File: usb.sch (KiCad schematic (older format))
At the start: 17 parts, among them J4 CONN_02X03, U1 LFE5U-85F-6BG381C, Y1 FNETHE025

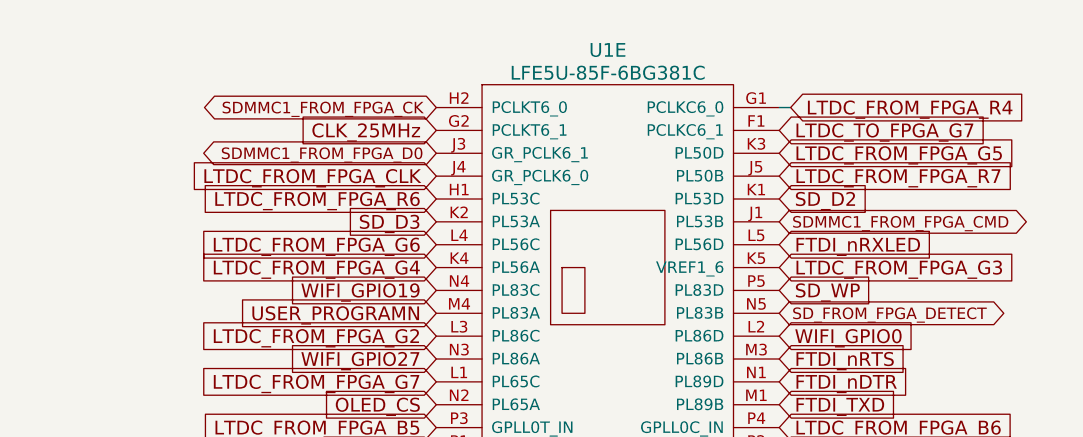
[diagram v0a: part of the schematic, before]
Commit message: Adding SPI from FPGA
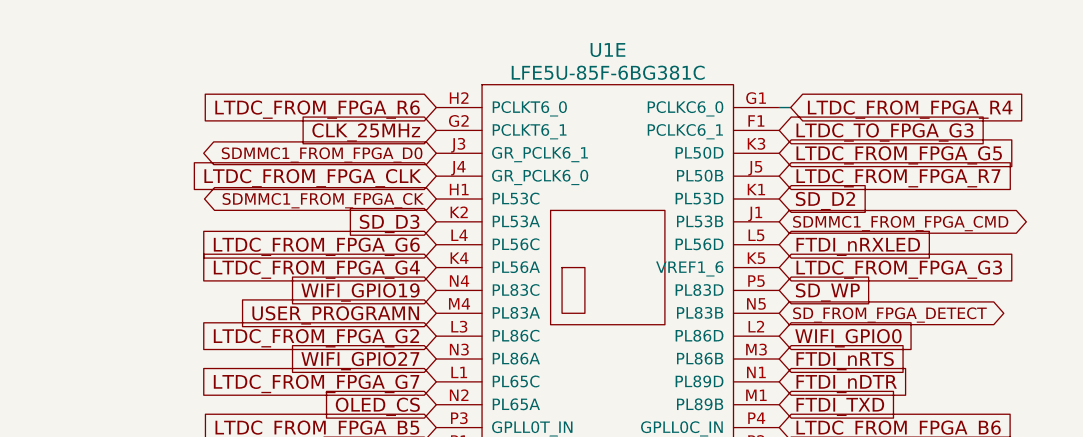
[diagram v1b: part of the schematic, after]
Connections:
- net LTDC_FROM_FPGA_R6: now also U1.H2 (PCLKT6_0); no longer U1.H1 (PL53C)
- net SDMMC1_FROM_FPGA_CK: now also U1.H1 (PL53C); no longer U1.H2 (PCLKT6_0)
- net LTDC_TO_FPGA_G7 renamed LTDC_TO_FPGA_G3
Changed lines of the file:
@@
 Text GLabel 10200 1350 2    60   Input ~ 0
 LTDC_FROM_FPGA_R4
-Text GLabel 8650 1750 0    60   Input ~ 0
+Text GLabel 8650 1350 0    60   Input ~ 0
 LTDC_FROM_FPGA_R6
 Text GLabel 8650 1650 0    60   Input ~ 0
@@
 Text GLabel 8650 1550 0    50   BiDi ~ 0
 SDMMC1_FROM_FPGA_D0
-Text GLabel 8650 1350 0    50   BiDi ~ 0
+Text GLabel 8650 1750 0    50   BiDi ~ 0
 SDMMC1_FROM_FPGA_CK
 Text GLabel 10150 1450 2    60   Input ~ 0
-LTDC_TO_FPGA_G7
+LTDC_TO_FPGA_G3
 $EndSCHEMATC

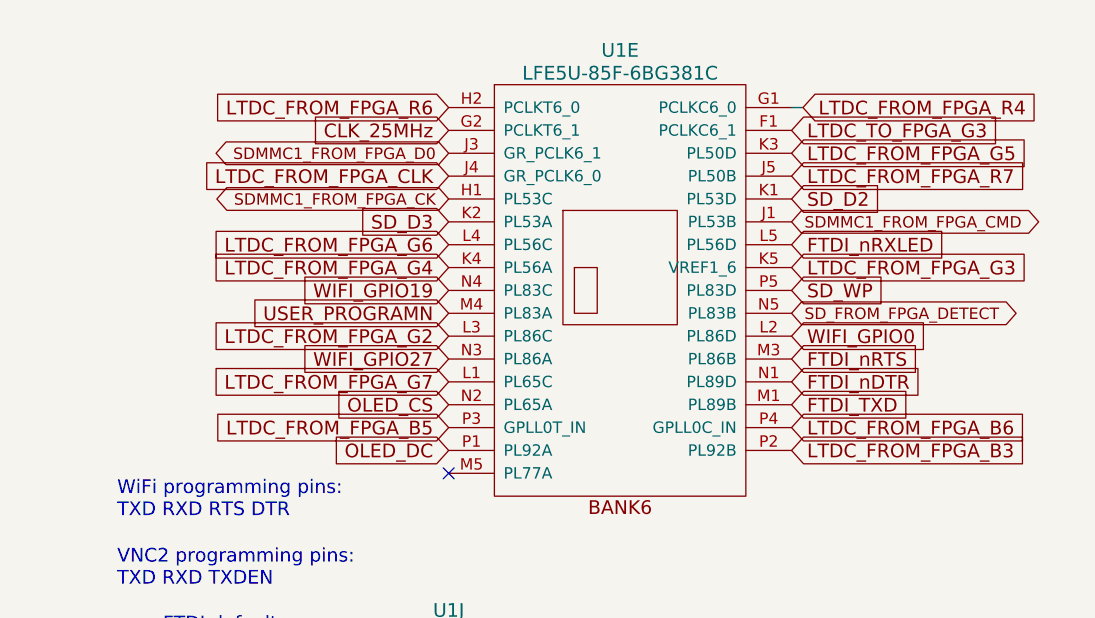
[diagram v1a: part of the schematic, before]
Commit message: Routing FPGA to LCD
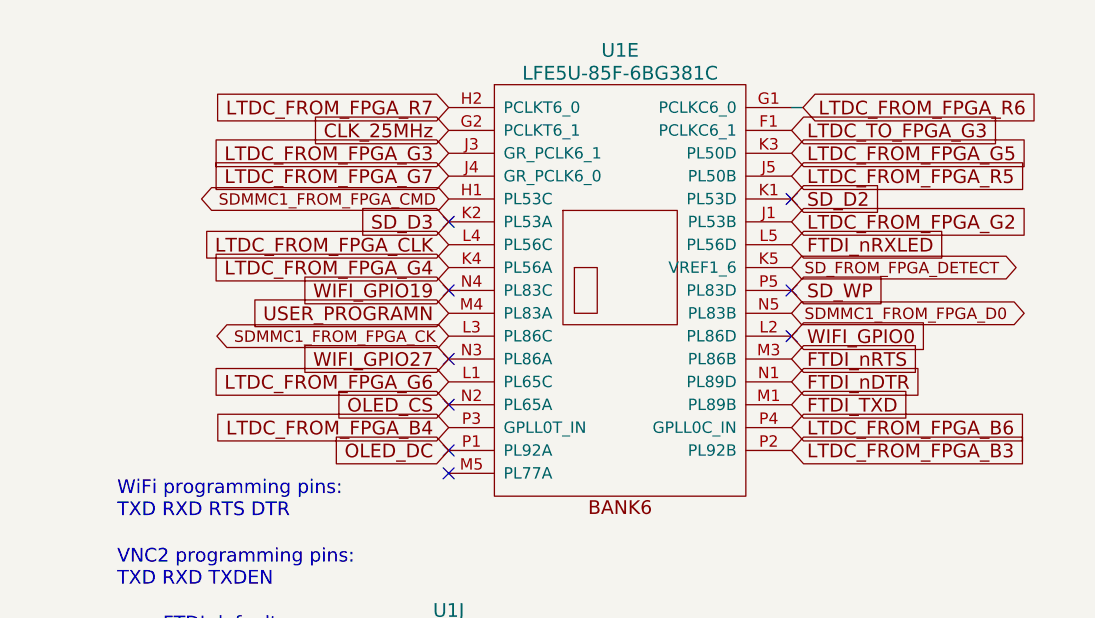
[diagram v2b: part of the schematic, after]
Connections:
- net LTDC_FROM_FPGA_R4 is gone; now on net LTDC_FROM_FPGA_R6: U1.G1 (PCLKC6_0)
- net LTDC_FROM_FPGA_CLK: now also U1.L4 (PL56C); no longer U1.J4 (GR_PCLK6_0)
- net LTDC_FROM_FPGA_G2: now also U1.J1 (PL53B); no longer U1.L3 (PL86C)
- net LTDC_FROM_FPGA_G3: now also U1.J3 (GR_PCLK6_1); no longer U1.K5 (VREF1_6)
- net LTDC_FROM_FPGA_G6: now also U1.L1 (PL65C); no longer U1.L4 (PL56C)
- net LTDC_FROM_FPGA_G7: now also U1.J4 (GR_PCLK6_0); no longer U1.L1 (PL65C)
- net LTDC_FROM_FPGA_R6: no longer U1.H2 (PCLKT6_0)
- net LTDC_FROM_FPGA_R7: now also U1.H2 (PCLKT6_0); no longer U1.J5 (PL50B)
- net SDMMC1_FROM_FPGA_CK: now also U1.L3 (PL86C); no longer U1.H1 (PL53C)
- net SDMMC1_FROM_FPGA_CMD: now also U1.H1 (PL53C); no longer U1.J1 (PL53B)
- net SDMMC1_FROM_FPGA_D0: now also U1.N5 (PL83B); no longer U1.J3 (GR_PCLK6_1)
- net SD_FROM_FPGA_DETECT: now also U1.K5 (VREF1_6); no longer U1.N5 (PL83B)
- net LTDC_FROM_FPGA_B5 renamed LTDC_FROM_FPGA_B4
- new net LTDC_FROM_FPGA_R5: U1.J5 (PL50B)
- no-connect marks 1 -> 9
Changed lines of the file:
@@
 LTDC_FROM_FPGA_B6
 Text GLabel 10200 1350 2    60   Input ~ 0
-LTDC_FROM_FPGA_R4
-Text GLabel 8650 1350 0    60   Input ~ 0
 LTDC_FROM_FPGA_R6
-Text GLabel 8650 1650 0    60   Input ~ 0
+Text GLabel 8650 1950 0    60   Input ~ 0
 LTDC_FROM_FPGA_CLK
-Text GLabel 8650 2550 0    60   Input ~ 0
-LTDC_FROM_FPGA_G7
-Text GLabel 8650 1950 0    60   Input ~ 0
-LTDC_FROM_FPGA_G6
 Text GLabel 10150 1550 2    60   Input ~ 0
 LTDC_FROM_FPGA_G5
-Text GLabel 10150 2050 2    60   Input ~ 0
-LTDC_FROM_FPGA_G3
-Text GLabel 8650 2350 0    60   Input ~ 0
+Text GLabel 10150 1850 2    60   Input ~ 0
 LTDC_FROM_FPGA_G2
-Text GLabel 8650 2750 0    60   Input ~ 0
-LTDC_FROM_FPGA_B5
 Wire Wire Line
 	10150 1350 10200 1350
 Text GLabel 8650 2050 0    60   Input ~ 0
 LTDC_FROM_FPGA_G4
+Text GLabel 8650 1350 0    60   Input ~ 0
+LTDC_FROM_FPGA_R7
+Text GLabel 8650 1750 0    50   BiDi ~ 0
+SDMMC1_FROM_FPGA_CMD
+Text GLabel 10150 2250 2    50   BiDi ~ 0
+SDMMC1_FROM_FPGA_D0
+Text GLabel 8650 2350 0    50   BiDi ~ 0
+SDMMC1_FROM_FPGA_CK
+NoConn ~ 10150 1750
+NoConn ~ 10150 2150
+NoConn ~ 10150 2350
+NoConn ~ 8650 2850
+NoConn ~ 8650 2650
+NoConn ~ 8650 2450
+NoConn ~ 8650 2150
+NoConn ~ 8650 1850
 Text GLabel 10150 1650 2    60   Input ~ 0
-LTDC_FROM_FPGA_R7
-Text GLabel 10150 2250 2    50   BiDi ~ 0
+LTDC_FROM_FPGA_R5
+Text GLabel 10150 2050 2    50   BiDi ~ 0
 SD_FROM_FPGA_DETECT
-Text GLabel 10150 1850 2    50   BiDi ~ 0
-SDMMC1_FROM_FPGA_CMD
-Text GLabel 8650 1550 0    50   BiDi ~ 0
-SDMMC1_FROM_FPGA_D0
-Text GLabel 8650 1750 0    50   BiDi ~ 0
-SDMMC1_FROM_FPGA_CK
 Text GLabel 10150 1450 2    60   Input ~ 0
 LTDC_TO_FPGA_G3
+Text GLabel 8650 1550 0    60   Input ~ 0
+LTDC_FROM_FPGA_G3
+Text GLabel 8650 1650 0    60   Input ~ 0
+LTDC_FROM_FPGA_G7
+Text GLabel 8650 2550 0    60   Input ~ 0
+LTDC_FROM_FPGA_G6
+Text GLabel 8650 2750 0    60   Input ~ 0
+LTDC_FROM_FPGA_B4
 $EndSCHEMATC

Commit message: Routing long signals
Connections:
- net FTDI_nDTR renamed SPI5_TO_FPGA_IRQ
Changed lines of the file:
@@
 Text GLabel 10150 2450 2    60   Input ~ 0
 FTDI_nRTS
-Text GLabel 10150 2550 2    60   Input ~ 0
-FTDI_nDTR
 Text GLabel 10150 2350 2    60   Input ~ 0
 WIFI_GPIO0
@@
 Text GLabel 8650 2750 0    60   Input ~ 0
 LTDC_FROM_FPGA_B4
+Text GLabel 10150 2550 2    50   BiDi ~ 0
+SPI5_TO_FPGA_IRQ
 $EndSCHEMATC

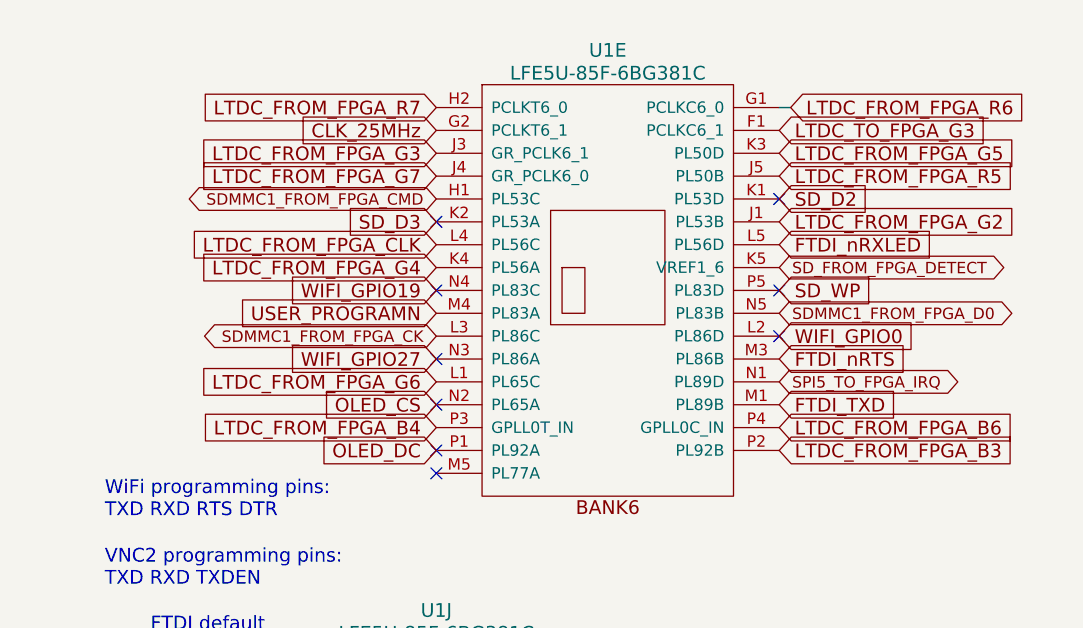
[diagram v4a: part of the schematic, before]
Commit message: Finish routing - removing CE and OpenHW number
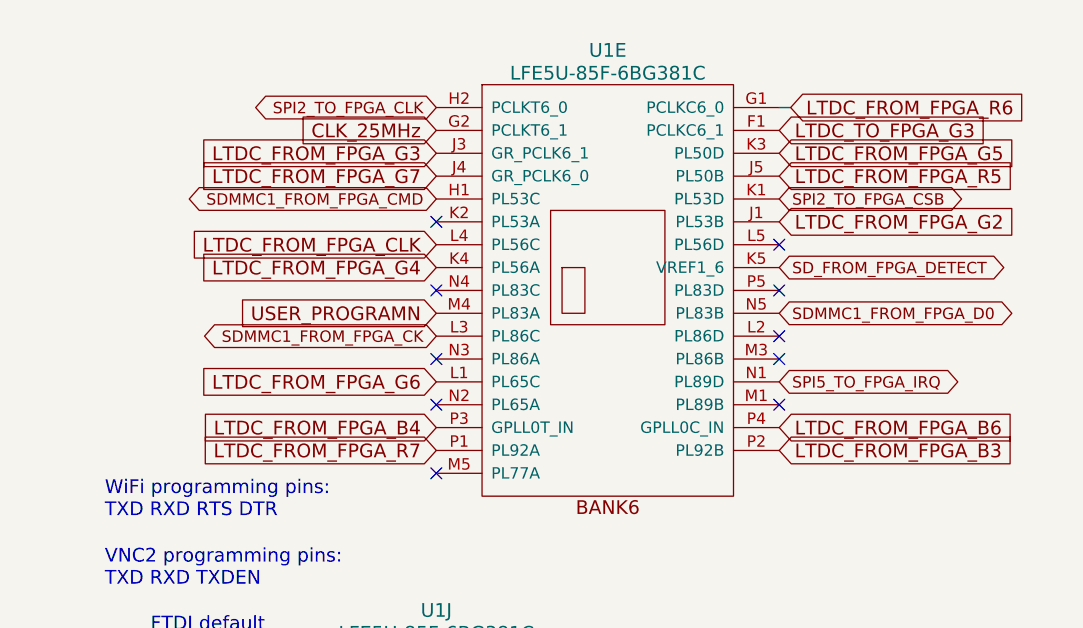
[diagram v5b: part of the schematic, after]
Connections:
- net OLED_DC is gone; now on net LTDC_FROM_FPGA_R7: U1.P1 (PL92A)
- net LTDC_FROM_FPGA_R7: no longer U1.H2 (PCLKT6_0)
- net FTDI_TXD: no longer names the net of U1.M1 (PL89B)
- net FTDI_nRTS: no longer names the net of U1.M3 (PL86B)
- net FTDI_nRXLED: no longer names the net of U1.L5 (PL56D)
- net OLED_CS: no longer names the net of U1.N2 (PL65A)
- net SD_D2 renamed SPI2_TO_FPGA_CSB
- net SD_D3: no longer names the net of U1.K2 (PL53A)
- net SD_WP: no longer names the net of U1.P5 (PL83D)
- net WIFI_GPIO0: no longer names the net of U1.L2 (PL86D)
- net WIFI_GPIO19: no longer names the net of U1.N4 (PL83C)
- net WIFI_GPIO27: no longer names the net of U1.N3 (PL86A)
- new net SPI2_TO_FPGA_CLK: U1.H2 (PCLKT6_0)
- no-connect marks 9 -> 10
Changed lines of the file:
@@
 Wire Wire Line
 	1800 2850 2150 2850
-Text GLabel 10150 2650 2    60   Input ~ 0
-FTDI_TXD
-Text GLabel 10150 2450 2    60   Input ~ 0
-FTDI_nRTS
-Text GLabel 10150 2350 2    60   Input ~ 0
-WIFI_GPIO0
-Text GLabel 8650 2850 0    60   Input ~ 0
-OLED_DC
-Text GLabel 8650 2650 0    60   Input ~ 0
-OLED_CS
-Text GLabel 10150 1750 2    60   Input ~ 0
-SD_D2
-Text GLabel 8650 1850 0    60   Input ~ 0
-SD_D3
-Text GLabel 10150 2150 2    60   Input ~ 0
-SD_WP
 Text Notes 7200 3150 0    60   ~ 0
 WiFi programming pins:\nTXD RXD RTS DTR
@@
 	1    0    0    -1
 $EndComp
-Text GLabel 8650 2150 0    60   Input ~ 0
-WIFI_GPIO19
-Text GLabel 8650 2450 0    60   Input ~ 0
-WIFI_GPIO27
 Text GLabel 1600 4850 0    60   Input ~ 0
 USB_FPGA_PULL_D+
@@
 USER_PROGRAMN
 NoConn ~ 8650 2950
-Text GLabel 10150 1950 2    60   Input ~ 0
-FTDI_nRXLED
 Text GLabel 10150 2850 2    60   Input ~ 0
 LTDC_FROM_FPGA_B3
@@
 Text GLabel 8650 2050 0    60   Input ~ 0
 LTDC_FROM_FPGA_G4
-Text GLabel 8650 1350 0    60   Input ~ 0
+Text GLabel 8650 2850 0    60   Input ~ 0
 LTDC_FROM_FPGA_R7
 Text GLabel 8650 1750 0    50   BiDi ~ 0
@@
 Text GLabel 8650 2350 0    50   BiDi ~ 0
 SDMMC1_FROM_FPGA_CK
-NoConn ~ 10150 1750
 NoConn ~ 10150 2150
 NoConn ~ 10150 2350
-NoConn ~ 8650 2850
 NoConn ~ 8650 2650
 NoConn ~ 8650 2450
@@
 Text GLabel 10150 2550 2    50   BiDi ~ 0
 SPI5_TO_FPGA_IRQ
+Text GLabel 10150 1750 2    50   BiDi ~ 0
+SPI2_TO_FPGA_CSB
+Text GLabel 8650 1350 0    50   BiDi ~ 0
+SPI2_TO_FPGA_CLK
+NoConn ~ 10150 1950
+NoConn ~ 10150 2450
+NoConn ~ 10150 2650
 $EndSCHEMATC

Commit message: V0.1
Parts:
- added JP1, JP2, JP3, JP4: Jumper_NC_Small, Capacitor_SMD:C_0402_1005Metric, symbol antena:Jumper_NC_Small
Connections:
- net JTAG_TCK: now also JP3.2
- net JTAG_TDI: now also JP1.2
- net JTAG_TDO: now also JP2.2
- net JTAG_TMS: now also JP4.2
- net SPI2_TO_FPGA_CLK: now also JP3.1
- new net DOUT2: JP4.1
- new net SPI2_TO_FPGA_MISO: JP1.1
- new net SPI2_TO_FPGA_MOSI: JP2.1
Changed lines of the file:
@@
 EESchema Schematic File Version 4
-LIBS:ulx3s-cache
-EELAYER 29 0
+EELAYER 30 0
 EELAYER END
 $Descr A4 11693 8268
@@
 NoConn ~ 10150 2450
 NoConn ~ 10150 2650
+$Comp
+L antena:Jumper_NC_Small JP?
+U 1 1 5FA6E3AF
+P 7550 4650
+AR Path="/58D6D507/5FA6E3AF" Ref="JP?"  Part="1"
+AR Path="/58D6BF46/5FA6E3AF" Ref="JP1"  Part="1"
+F 0 "JP1" H 7550 4862 50  0000 C CNN
+F 1 "Jumper_NC_Small" H 7550 4771 50  0000 C CNN
+F 2 "Capacitor_SMD:C_0402_1005Metric" H 7550 4650 50  0001 C CNN
+F 3 "~" H 7550 4650 50  0001 C CNN
+	1    7550 4650
+	1    0    0    -1
+$EndComp
+$Comp
+L antena:Jumper_NC_Small JP?
+U 1 1 5FA6E3B5
+P 7550 4950
+AR Path="/58D6D507/5FA6E3B5" Ref="JP?"  Part="1"
+AR Path="/58D6BF46/5FA6E3B5" Ref="JP2"  Part="1"
+F 0 "JP2" H 7550 5162 50  0000 C CNN
+F 1 "Jumper_NC_Small" H 7550 5071 50  0000 C CNN
+F 2 "Capacitor_SMD:C_0402_1005Metric" H 7550 4950 50  0001 C CNN
+F 3 "~" H 7550 4950 50  0001 C CNN
+	1    7550 4950
+	1    0    0    -1
+$EndComp
+$Comp
+L antena:Jumper_NC_Small JP?
+U 1 1 5FA6E3BB
+P 7550 5250
+AR Path="/58D6D507/5FA6E3BB" Ref="JP?"  Part="1"
+AR Path="/58D6BF46/5FA6E3BB" Ref="JP3"  Part="1"
+F 0 "JP3" H 7550 5462 50  0000 C CNN
+F 1 "Jumper_NC_Small" H 7550 5371 50  0000 C CNN
+F 2 "Capacitor_SMD:C_0402_1005Metric" H 7550 5250 50  0001 C CNN
+F 3 "~" H 7550 5250 50  0001 C CNN
+	1    7550 5250
+	1    0    0    -1
+$EndComp
+$Comp
+L antena:Jumper_NC_Small JP?
+U 1 1 5FA6E3C1
+P 7550 5550
+AR Path="/58D6D507/5FA6E3C1" Ref="JP?"  Part="1"
+AR Path="/58D6BF46/5FA6E3C1" Ref="JP4"  Part="1"
+F 0 "JP4" H 7550 5762 50  0000 C CNN
+F 1 "Jumper_NC_Small" H 7550 5671 50  0000 C CNN
+F 2 "Capacitor_SMD:C_0402_1005Metric" H 7550 5550 50  0001 C CNN
+F 3 "~" H 7550 5550 50  0001 C CNN
+	1    7550 5550
+	1    0    0    -1
+$EndComp
+Text GLabel 7450 4650 0    50   BiDi ~ 0
+SPI2_TO_FPGA_MISO
+Text GLabel 7450 4950 0    50   BiDi ~ 0
+SPI2_TO_FPGA_MOSI
+Text GLabel 7450 5250 0    50   BiDi ~ 0
+SPI2_TO_FPGA_CLK
+Text GLabel 7450 5550 0    50   BiDi ~ 0
+DOUT2
+Text GLabel 7650 5250 2    60   Input ~ 0
+JTAG_TCK
+Text GLabel 7650 5550 2    60   Input ~ 0
+JTAG_TMS
+Text GLabel 7650 4650 2    60   Input ~ 0
+JTAG_TDI
+Text GLabel 7650 4950 2    60   Input ~ 0
+JTAG_TDO
 $EndSCHEMATC
